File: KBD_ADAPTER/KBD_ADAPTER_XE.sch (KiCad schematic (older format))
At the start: 2 parts, among them J1 Conn_01x24, J2 Conn_02x17_Counter_Clockwise

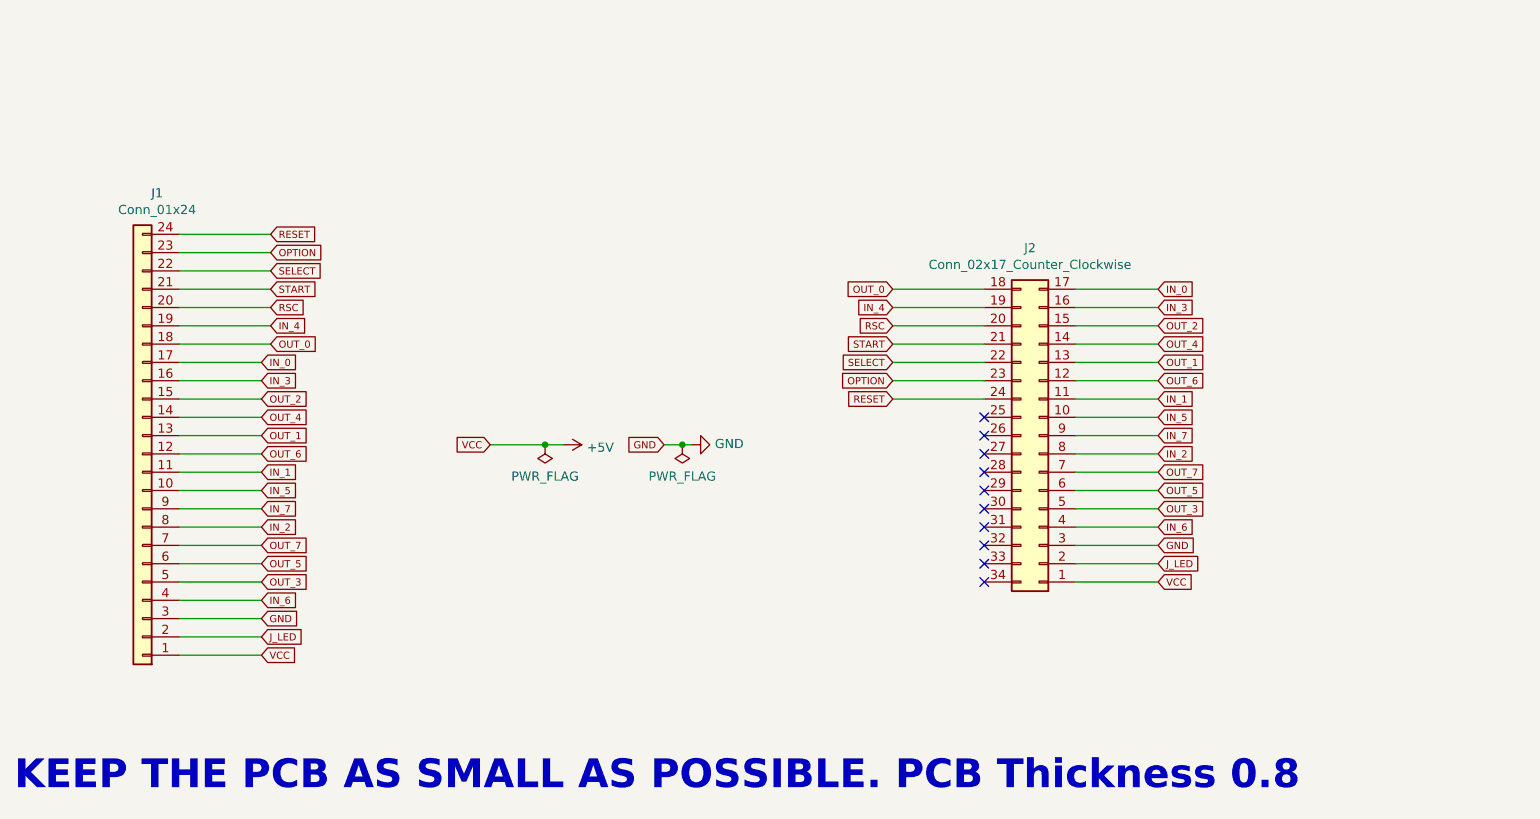
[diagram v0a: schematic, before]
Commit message: New FPC cable. No Flat Ribbon. It was too big!
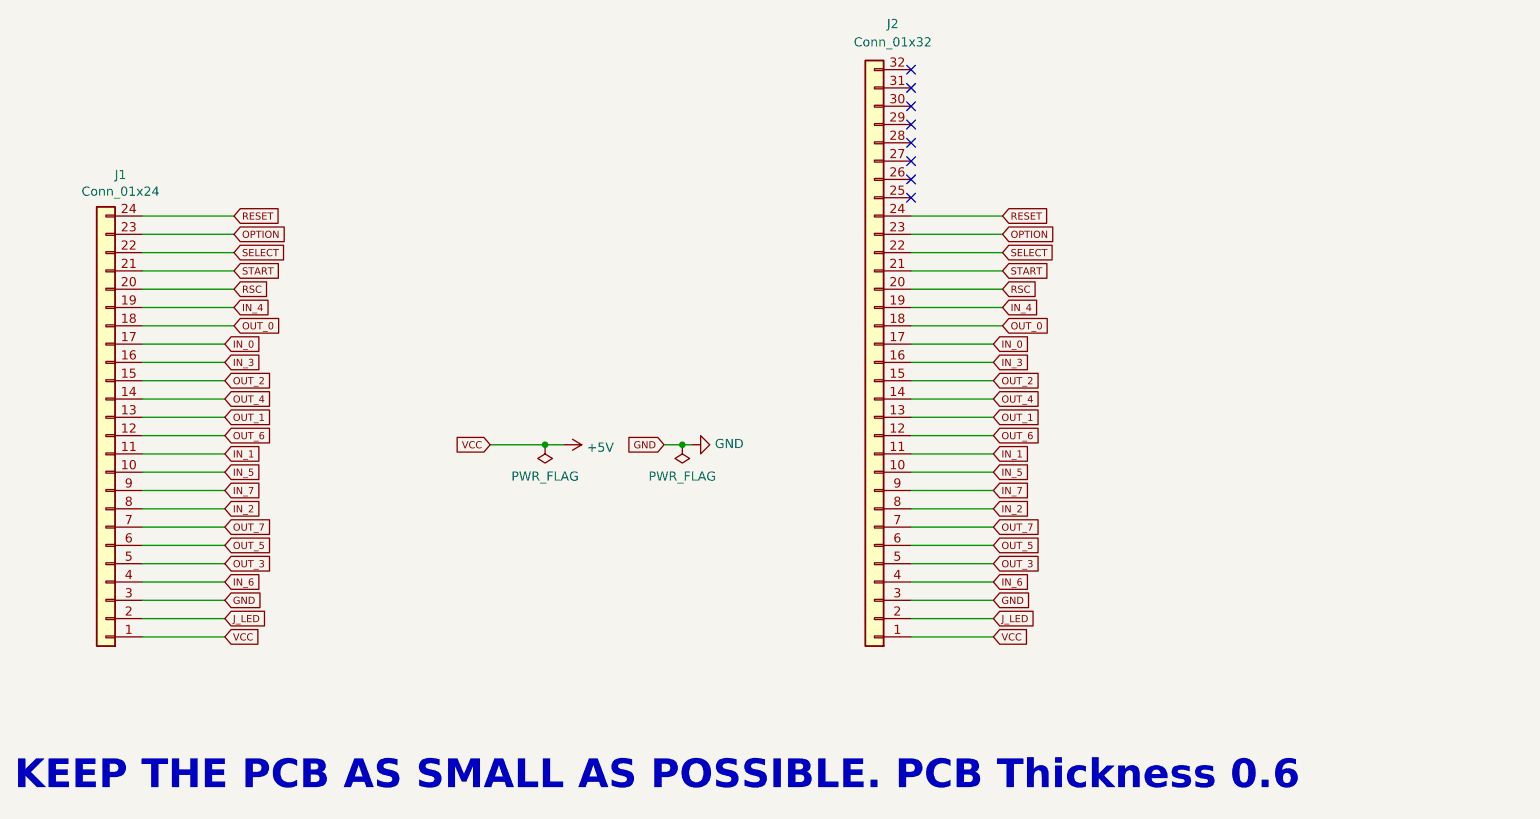
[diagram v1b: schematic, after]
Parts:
- removed J2: Conn_02x17_Counter_Clockwise, RetroBitLab:IDC-Header_2x17_P2.54mm_Vertical_Lock, symbol Connector_Generic:Conn_02x17_Counter_Clockwise
- added J2: Conn_01x32, RetroBitLab:FFC-1.25mm-RA-5204403245, symbol Connector_Generic:Conn_01x32
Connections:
- net +5V: now also J2.1 (Pin_1)
- net GND: now also J2.3 (Pin_3)
- net IN_0: now also J2.17 (Pin_17)
- net IN_1: now also J2.11 (Pin_11)
- net IN_2: now also J2.8 (Pin_8)
- net IN_3: now also J2.16 (Pin_16)
- net IN_4: now also J2.19 (Pin_19)
- net IN_5: now also J2.10 (Pin_10)
- net IN_6: now also J2.4 (Pin_4)
- net IN_7: now also J2.9 (Pin_9)
- net J_LED: now also J2.2 (Pin_2)
- net OPTION: now also J2.23 (Pin_23)
- net OUT_0: now also J2.18 (Pin_18)
- net OUT_1: now also J2.13 (Pin_13)
- net OUT_2: now also J2.15 (Pin_15)
- net OUT_3: now also J2.5 (Pin_5)
- net OUT_4: now also J2.14 (Pin_14)
- net OUT_5: now also J2.6 (Pin_6)
- net OUT_6: now also J2.12 (Pin_12)
- net OUT_7: now also J2.7 (Pin_7)
- net RESET: now also J2.24 (Pin_24)
- net RSC: now also J2.20 (Pin_20)
- net SELECT: now also J2.22 (Pin_22)
- net START: now also J2.21 (Pin_21)
- no-connect marks 10 -> 8
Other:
- note added: "KEEP THE PCB AS SMALL AS POSSIBLE. PCB Thickness 0.6"
- note removed: "KEEP THE PCB AS SMALL AS POSSIBLE. PCB Thickness 0.8"
- moved on the sheet: J1

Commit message: Straight vertical Molex Connector: RA52045-3245 (End Of Life!!)
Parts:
- J2: footprint RetroBitLab:FFC-1.25mm-RA-5204403245 -> RetroBitLab:MOLEX-FFC-1.25mm-RA-52045-3245
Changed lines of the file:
@@
 F 0 "J2" H 6800 1950 50  0000 C CNN
 F 1 "Conn_01x32" H 6800 2050 50  0000 C CNN
-F 2 "RetroBitLab:FFC-1.25mm-RA-5204403245" H 6900 3800 50  0001 C CNN
+F 2 "RetroBitLab:MOLEX-FFC-1.25mm-RA-52045-3245" H 6900 3800 50  0001 C CNN
 F 3 "~" H 6900 3800 50  0001 C CNN
 	1    6900 3800
